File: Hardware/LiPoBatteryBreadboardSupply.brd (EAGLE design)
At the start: 55 x 15.2 mm, 20 parts

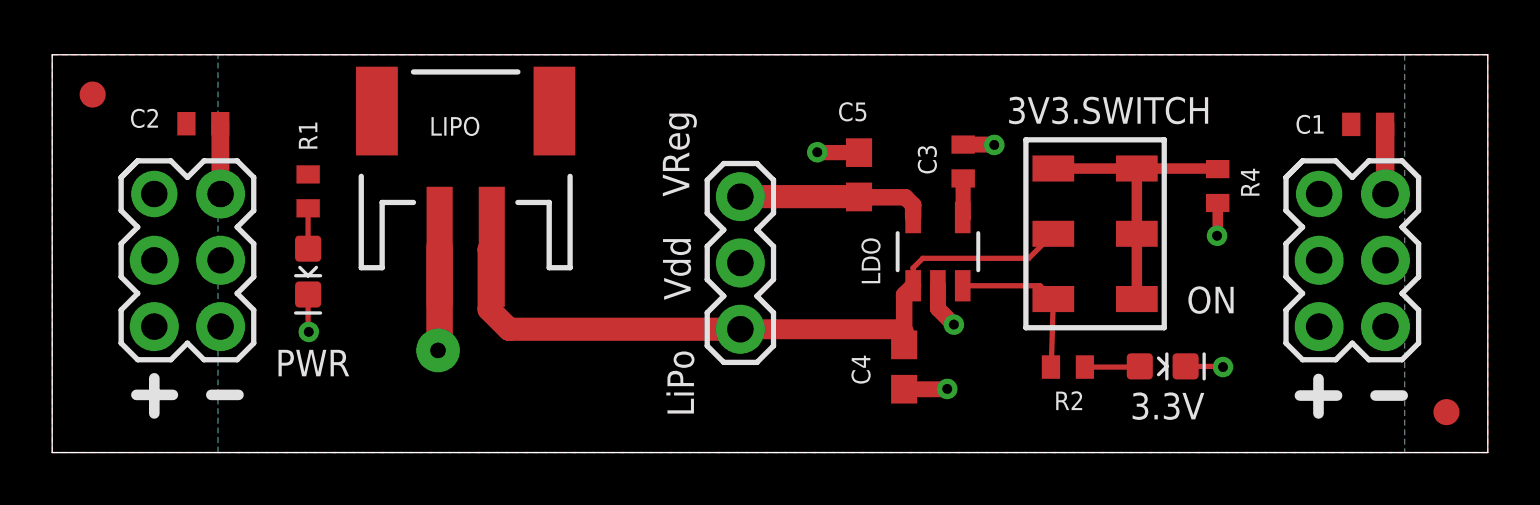
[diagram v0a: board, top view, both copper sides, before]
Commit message: changes to the silkscreen and changes to the BOM
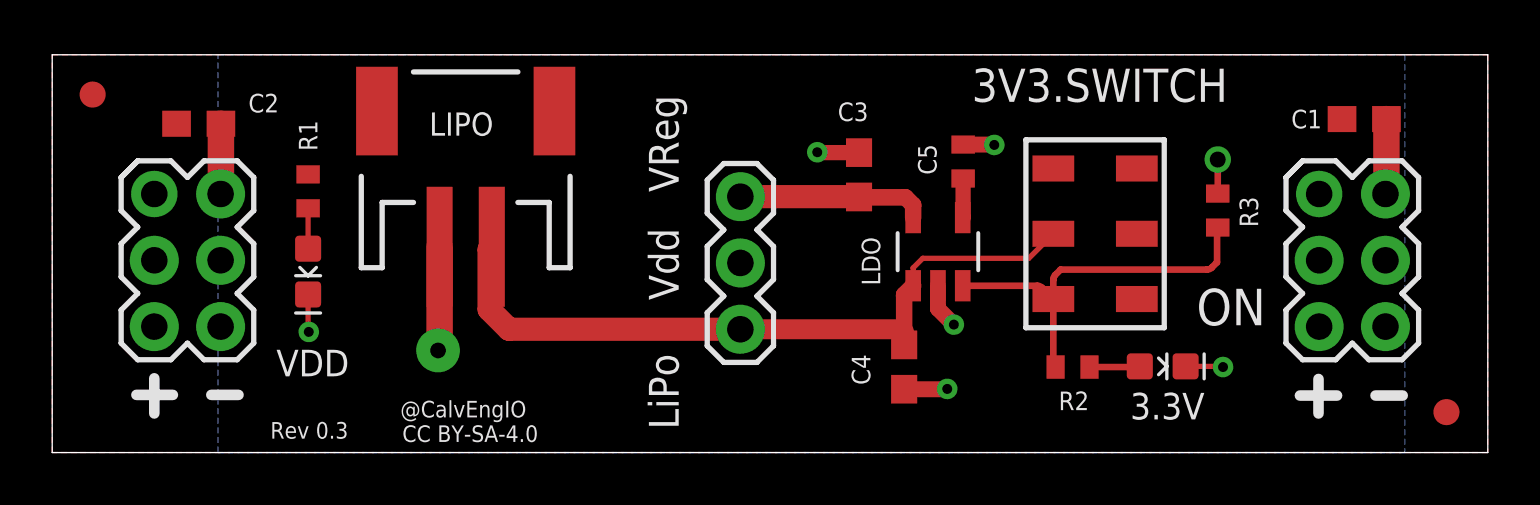
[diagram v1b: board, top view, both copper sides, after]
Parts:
- removed R4: 10k, resistor:R0402
- added R3: 100k, resistor:R0402
- added U$1: HANDLE.1HANDLE.025, CalvEngIO-Logos:HANDLE.025
- C1, C2: device resistor:C0402 -> CalvEngIO-Passives:C0603
- C3: value 100pF -> 2.2u; device resistor:C0402 -> resistor:C0603
- C4: value 1u -> 2.2u
- C5: value 2.2u -> 100pF; device resistor:C0603 -> resistor:C0402
- U$6: value LOGO.08 -> HANDLE.1HANDLE.08; device CalvEngIO-Logo:LOGO.08 -> CalvEngIO-Logos:HANDLE.08
- moved C3 4.02 mm to (30.9, 10.6)
- moved C5 4.02 mm to (34.9, 11.2)
- moved C1 0.25 mm to (50.3, 12.8)
- moved R2 0.18 mm to (39.1, 3.28)
- moved C2 0.18 mm to (5.61, 12.6)
- renumbered PWR to VDD
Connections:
- removed net N$3: 3V3.SWITCH.3, 3V3.SWITCH.5, 3V3.SWITCH.6, 3V3.SWITCH.7, R4.2
- net 3.3V: now also C3.1; no longer C5.1
- net EN: now also R3.2
- net GND: now also R3.1; no longer R4.1
- net N$4: now also C5.1; no longer C3.1
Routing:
- net N$3: track 11.3 -> 0.00 mm
- net EN: track 6.40 -> 15.2 mm
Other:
- board text added: "CC BY-SA-4.0"
- board text added: "Rev 0.3"

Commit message: changes to BOM and change in value of Cbypass on regulator in schematic
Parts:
- C5: value 100pF -> 47pF
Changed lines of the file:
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@@
 <layer number="37" name="tTest" color="7" fill="1" visible="no" active="yes"/>
 <layer number="38" name="bTest" color="7" fill="1" visible="no" active="yes"/>
-<layer number="39" name="tKeepout" color="4" fill="11" visible="yes" active="yes"/>
-<layer number="40" name="bKeepout" color="1" fill="11" visible="yes" active="yes"/>
-<layer number="41" name="tRestrict" color="4" fill="10" visible="yes" active="yes"/>
-<layer number="42" name="bRestrict" color="1" fill="10" visible="yes" active="yes"/>
-<layer number="43" name="vRestrict" color="2" fill="10" visible="yes" active="yes"/>
-<layer number="44" name="Drills" color="7" fill="1" visible="no" active="yes"/>
-<layer number="45" name="Holes" color="7" fill="1" visible="no" active="yes"/>
-<layer number="46" name="Milling" color="3" fill="1" visible="no" active="yes"/>
-<layer number="47" name="Measures" color="7" fill="1" visible="no" active="yes"/>
+<layer number="39" name="tKeepout" color="4" fill="11" visible="no" active="yes"/>
+<layer number="40" name="bKeepout" color="1" fill="11" visible="no" active="yes"/>
+<layer number="41" name="tRestrict" color="4" fill="10" visible="no" active="yes"/>
+<layer number="42" name="bRestrict" color="1" fill="10" visible="no" active="yes"/>
+<layer number="43" name="vRestrict" color="2" fill="10" visible="no" active="yes"/>
+<layer number="44" name="Drills" color="7" fill="1" visible="yes" active="yes"/>
+<layer number="45" name="Holes" color="7" fill="1" visible="yes" active="yes"/>
+<layer number="46" name="Milling" color="3" fill="1" visible="yes" active="yes"/>
+<layer number="47" name="Measures" color="7" fill="1" visible="yes" active="yes"/>
 <layer number="48" name="Document" color="7" fill="1" visible="yes" active="yes"/>
 <layer number="49" name="Reference" color="7" fill="1" visible="yes" active="yes"/>
@@
 <attribute name="VALUE" x="36.9824" y="5.9182" size="0.889" layer="27" ratio="10" rot="R90"/>
 </element>
-<element name="C5" library="resistor" package="C0402" value="100pF" x="34.8996" y="11.1506" smashed="yes" rot="R90">
+<element name="C5" library="resistor" package="C0402" value="47pF" x="34.8996" y="11.1506" smashed="yes" rot="R90">
 <attribute name="NAME" x="33.8836" y="10.6426" size="0.7112" layer="25" rot="R90"/>
 <attribute name="VALUE" x="36.8046" y="10.5156" size="0.889" layer="27" rot="R90"/>
